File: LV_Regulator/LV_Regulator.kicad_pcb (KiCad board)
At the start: 2 copper layers, 0 parts

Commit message: Changes of PCB and Schematic files for the LV_Regulator
Removed old LDOs, added new LDOs, defined initial pcb size and I/O ports
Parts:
- added C13: ---, Capacitor_SMD:C_1206_3216Metric, F.Cu at (-29.2, 163.0)
- added C14: ---, Capacitor_SMD:C_1206_3216Metric, F.Cu at (-29.2, 166.3)
- added C15: ---, Capacitor_SMD:C_1206_3216Metric, F.Cu at (-29.2, 169.7)
- added C16: ---, Capacitor_SMD:C_1206_3216Metric, F.Cu at (-29.2, 173.0)
- added C17: 0.1uF, Capacitor_SMD:C_1206_3216Metric, F.Cu at (-29.2, 176.4)
- added C18: 100nF, Capacitor_SMD:C_1206_3216Metric, F.Cu at (-29.2, 179.7)
- added C19: 100nF, Capacitor_SMD:C_1206_3216Metric, F.Cu at (-23.5, 163.0)
- added C20: 100nF, Capacitor_SMD:C_1206_3216Metric, F.Cu at (-23.5, 166.3)
- added C21: 10uF, Capacitor_SMD:C_1206_3216Metric, F.Cu at (-23.5, 169.7)
- added C22: 100nF, Capacitor_SMD:C_1206_3216Metric, F.Cu at (-23.5, 173.0)
- added C23: 100nF, Capacitor_SMD:C_1206_3216Metric, F.Cu at (-23.5, 176.4)
- added C24: 100nF, Capacitor_SMD:C_1206_3216Metric, F.Cu at (-34.8, 126.9)
- added C25: 80uF, Capacitor_SMD:C_1206_3216Metric, F.Cu at (-34.8, 130.3)
- added C26: 40uF, Capacitor_SMD:C_1206_3216Metric, F.Cu at (-34.8, 133.6)
- added C27: 100nF, Capacitor_SMD:C_1206_3216Metric, F.Cu at (-34.8, 137.0)
- added C28: 100nF, Capacitor_SMD:C_1206_3216Metric, F.Cu at (-34.8, 140.3)
- added C29: 100nF, Capacitor_SMD:C_1206_3216Metric, F.Cu at (-34.8, 143.7)
- added C30: 40uF, Capacitor_SMD:C_1206_3216Metric, F.Cu at (-34.8, 147.0)
- added C31: 160uF, ul_UCZ1J181MNQ1MS:CAP_UCD_12P5X13P5_NCH, F.Cu at (-0.66, 151.6)
- added C32: 1uF, Capacitor_SMD:C_1206_3216Metric, F.Cu at (-34.8, 150.4)
- added C33: 1uF, Capacitor_SMD:C_1206_3216Metric, F.Cu at (-34.8, 153.7)
- added D6: LED, Diode_SMD:D_1206_3216Metric_Pad1.42x1.75mm_HandSolder, F.Cu at (-21.0, 146.8)
- added D7: LED, Diode_SMD:D_1206_3216Metric_Pad1.42x1.75mm_HandSolder, F.Cu at (-21.0, 150.2)
- added J1: 430450400, microfit-4pin:CONN_SD-43045-001_04_MOL, F.Cu at (208.3, 127.4)
- added J2: 430450800, microfit-8pin:CONN_SD-43045-001_08_MOL, F.Cu at (212.4, 63.0)
- added J3: 430450400, microfit-4pin:CONN_SD-43045-001_04_MOL, F.Cu at (188.8, 127.4)
- added J4: 430450800, microfit-8pin:CONN_SD-43045-001_08_MOL, F.Cu at (81.6, 72.0)
- added J6: 2169890001, USB_C:MOLEX_2169890001, F.Cu at (218.5, 107.5)
- added JP1: BOOT0, Jumper:SolderJumper-3_P1.3mm_Open_Pad1.0x1.5mm, F.Cu at (-34.8, 163.1)
- added JP10: SolderJumper_3_Open, Jumper:SolderJumper-3_P1.3mm_Open_Pad1.0x1.5mm, F.Cu at (10.5, 145.7)
- added JP11: SolderJumper_3_Open, Jumper:SolderJumper-3_P1.3mm_Open_Pad1.0x1.5mm, F.Cu at (10.5, 149.6)
- added JP12: SolderJumper_3_Open, Jumper:SolderJumper-3_P1.3mm_Open_Pad1.0x1.5mm, F.Cu at (10.5, 153.4)
- added JP13: SolderJumper_3_Open, Jumper:SolderJumper-3_P1.3mm_Open_Pad1.0x1.5mm, F.Cu at (10.5, 157.2)
- added JP2: ADR3, Jumper:SolderJumper-3_P1.3mm_Open_Pad1.0x1.5mm, F.Cu at (-34.8, 166.9)
- added JP3: BOOT1, Jumper:SolderJumper-3_P1.3mm_Open_Pad1.0x1.5mm, F.Cu at (-34.8, 170.8)
- added JP4: ADR2, Jumper:SolderJumper-3_P1.3mm_Open_Pad1.0x1.5mm, F.Cu at (-34.8, 174.6)
- added JP5: RESET, Jumper:SolderJumper-2_P1.3mm_Open_Pad1.0x1.5mm, F.Cu at (-29.8, 189.8)
- added JP6: ADR1, Jumper:SolderJumper-3_P1.3mm_Open_Pad1.0x1.5mm, F.Cu at (-34.8, 178.4)
- added JP7: ADR3, Jumper:SolderJumper-3_P1.3mm_Open_Pad1.0x1.5mm, F.Cu at (-34.8, 182.3)
- added JP8: ADR3, Jumper:SolderJumper-3_P1.3mm_Open_Pad1.0x1.5mm, F.Cu at (-34.8, 186.1)
- added L1: 10uH, Inductor_SMD:L_APV_APH1770, F.Cu at (0.30, 134.6)
- added Q1: BC807, Package_TO_SOT_SMD:SOT-23W_Handsoldering, F.Cu at (37.9, 122.0)
- added R10: 1M, Resistor_SMD:R_1206_3216Metric, F.Cu at (-29.2, 126.9)
- added R11: 10, Resistor_SMD:R_1206_3216Metric, F.Cu at (-29.2, 130.2)
- added R118: 27R, Resistor_SMD:R_1206_3216Metric_Pad1.30x1.75mm_HandSolder, F.Cu at (-17.7, 163.0)
- added R119: 27R, Resistor_SMD:R_1206_3216Metric_Pad1.30x1.75mm_HandSolder, F.Cu at (-17.7, 166.3)
- added R12: 5m, Resistor_SMD:R_1206_3216Metric, F.Cu at (-29.2, 133.5)
- added R120: 1K5, Resistor_SMD:R_1206_3216Metric_Pad1.30x1.75mm_HandSolder, F.Cu at (-17.7, 169.6)
- added R121: 5K1, Resistor_SMD:R_1206_3216Metric_Pad1.30x1.75mm_HandSolder, F.Cu at (-17.7, 172.9)
- added R122: 5K1, Resistor_SMD:R_1206_3216Metric_Pad1.30x1.75mm_HandSolder, F.Cu at (-17.7, 176.2)
- added R13: 10, Resistor_SMD:R_1206_3216Metric, F.Cu at (-29.2, 136.8)
- added R14: 1M, Resistor_SMD:R_1206_3216Metric, F.Cu at (-29.2, 140.2)
- added R15: 311k, Resistor_SMD:R_1206_3216Metric, F.Cu at (-29.2, 143.5)
- added R16: 22k, Resistor_SMD:R_1206_3216Metric, F.Cu at (-23.6, 126.9)
- added R31: 67k, Resistor_SMD:R_1206_3216Metric, F.Cu at (-23.6, 130.2)
- added R32: 57k, Resistor_SMD:R_1206_3216Metric, F.Cu at (-23.6, 133.5)
- added R33: 50k, Resistor_SMD:R_1206_3216Metric, F.Cu at (-23.6, 136.8)
- added R34: 100k, Resistor_SMD:R_1206_3216Metric, F.Cu at (-23.6, 140.2)
- added R35: 80k, Resistor_SMD:R_1206_3216Metric, F.Cu at (-23.6, 143.5)
- added R36: 132k, Resistor_SMD:R_1206_3216Metric, F.Cu at (-18.0, 126.9)
- added R37: 115k, Resistor_SMD:R_1206_3216Metric, F.Cu at (-18.0, 130.2)
- added R38: 1k, Resistor_SMD:R_1206_3216Metric, F.Cu at (-18.0, 133.5)
- added R39: 22k, Resistor_SMD:R_1206_3216Metric, F.Cu at (-18.0, 136.8)
- added R40: 1k, Resistor_SMD:R_1206_3216Metric, F.Cu at (-18.0, 140.2)
- added R41: 10k, Resistor_SMD:R_1206_3216Metric, F.Cu at (-18.0, 143.5)
- added R42: 10k, Resistor_SMD:R_1206_3216Metric, F.Cu at (-12.4, 126.9)
- added R43: ---, Resistor_SMD:R_1206_3216Metric, F.Cu at (-12.4, 130.2)
- added R44: ---, Resistor_SMD:R_1206_3216Metric, F.Cu at (-12.4, 133.5)
- added R45: ---, Resistor_SMD:R_1206_3216Metric, F.Cu at (-12.4, 136.8)
- added R46: ---, Resistor_SMD:R_1206_3216Metric, F.Cu at (-12.4, 140.2)
- added R47: 2.2k, Resistor_SMD:R_1206_3216Metric, F.Cu at (-12.4, 143.5)
- added U1: ADM2483xRW, Package_SO:SOIC-16W_7.5x10.3mm_P1.27mm, F.Cu at (178.5, 111.0)
- added U10: 25CSM04xxSN, Package_SO:SOIC-8_3.9x4.9mm_P1.27mm, F.Cu at (174.5, 94.5)
- added U2: MCP1826T-ADJE_DC, MCP1826T-ADJE_DC:SOT230P700X180-6N, F.Cu at (3.10, 165.2)
- added U3: MCP1826T-ADJE_DC, MCP1826T-ADJE_DC:SOT230P700X180-6N, F.Cu at (3.10, 173.1)
- added U4: STM32F103C8Tx, Package_QFP:LQFP-48_7x7mm_P0.5mm, F.Cu at (195.0, 92.5)
- added U5: BQ25858QWRRVRQ1, ul_BQ25858QWRRVRQ1:RRV0036B-IPC_A, F.Cu at (45.5, 167.0)
- added U6: CSD19506KTT, CSD19506KTT:DDPAK&slash_TO-263_KTT_TEX, F.Cu at (-31.7, 114.6)
- added U7: CSD19506KTT, CSD19506KTT:DDPAK&slash_TO-263_KTT_TEX, F.Cu at (-19.8, 114.6)
- added U8: CSD19506KTT, CSD19506KTT:DDPAK&slash_TO-263_KTT_TEX, F.Cu at (-7.86, 114.6)
- added U9: CSD19506KTT, CSD19506KTT:DDPAK&slash_TO-263_KTT_TEX, F.Cu at (4.06, 114.6)
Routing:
- added copper zone on B.Cu, net (none)
- added copper zone on F.Cu, net (none)
- added copper zone on In1.Cu, net (none)
- added copper zone on In2.Cu, net (none)
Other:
- board outline added: 150 x 100 mm
- copper layers 2 -> 4

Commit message: PCB Layout definitions part 2
Added isolation keepouts
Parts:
- removed C13, C14, C15, C16: ---, Capacitor_SMD:C_1206_3216Metric
- removed C17: 0.1uF, Capacitor_SMD:C_1206_3216Metric
- removed C18, C19, C20, C22, C23, C24, C27, C28, C29: 100nF, Capacitor_SMD:C_1206_3216Metric
- removed C21: 10uF, Capacitor_SMD:C_1206_3216Metric
- removed C25: 80uF, Capacitor_SMD:C_1206_3216Metric
- removed C26, C30: 40uF, Capacitor_SMD:C_1206_3216Metric
- removed C31: 160uF, ul_UCZ1J181MNQ1MS:CAP_UCD_12P5X13P5_NCH
- removed C32, C33: 1uF, Capacitor_SMD:C_1206_3216Metric
- removed D6, D7: LED, Diode_SMD:D_1206_3216Metric_Pad1.42x1.75mm_HandSolder
- removed J1, J3: 430450400, microfit-4pin:CONN_SD-43045-001_04_MOL
- removed J2, J4: 430450800, microfit-8pin:CONN_SD-43045-001_08_MOL
- removed J6: 2169890001, USB_C:MOLEX_2169890001
- removed JP1: BOOT0, Jumper:SolderJumper-3_P1.3mm_Open_Pad1.0x1.5mm
- removed JP10, JP11, JP12, JP13: SolderJumper_3_Open, Jumper:SolderJumper-3_P1.3mm_Open_Pad1.0x1.5mm
- removed JP2, JP7, JP8: ADR3, Jumper:SolderJumper-3_P1.3mm_Open_Pad1.0x1.5mm
- removed JP3: BOOT1, Jumper:SolderJumper-3_P1.3mm_Open_Pad1.0x1.5mm
- removed JP4: ADR2, Jumper:SolderJumper-3_P1.3mm_Open_Pad1.0x1.5mm
- removed JP5: RESET, Jumper:SolderJumper-2_P1.3mm_Open_Pad1.0x1.5mm
- removed JP6: ADR1, Jumper:SolderJumper-3_P1.3mm_Open_Pad1.0x1.5mm
- removed L1: 10uH, Inductor_SMD:L_APV_APH1770
- removed Q1: BC807, Package_TO_SOT_SMD:SOT-23W_Handsoldering
- removed R10, R14: 1M, Resistor_SMD:R_1206_3216Metric
- removed R11, R13: 10, Resistor_SMD:R_1206_3216Metric
- removed R118, R119: 27R, Resistor_SMD:R_1206_3216Metric_Pad1.30x1.75mm_HandSolder
- removed R12: 5m, Resistor_SMD:R_1206_3216Metric
- removed R120: 1K5, Resistor_SMD:R_1206_3216Metric_Pad1.30x1.75mm_HandSolder
- removed R121, R122: 5K1, Resistor_SMD:R_1206_3216Metric_Pad1.30x1.75mm_HandSolder
- removed R15: 311k, Resistor_SMD:R_1206_3216Metric
- removed R16, R39: 22k, Resistor_SMD:R_1206_3216Metric
- removed R31: 67k, Resistor_SMD:R_1206_3216Metric
- removed R32: 57k, Resistor_SMD:R_1206_3216Metric
- removed R33: 50k, Resistor_SMD:R_1206_3216Metric
- removed R34: 100k, Resistor_SMD:R_1206_3216Metric
- removed R35: 80k, Resistor_SMD:R_1206_3216Metric
- removed R36: 132k, Resistor_SMD:R_1206_3216Metric
- removed R37: 115k, Resistor_SMD:R_1206_3216Metric
- removed R38, R40: 1k, Resistor_SMD:R_1206_3216Metric
- removed R41, R42: 10k, Resistor_SMD:R_1206_3216Metric
- removed R43, R44, R45, R46: ---, Resistor_SMD:R_1206_3216Metric
- removed R47: 2.2k, Resistor_SMD:R_1206_3216Metric
- removed U1: ADM2483xRW, Package_SO:SOIC-16W_7.5x10.3mm_P1.27mm
- removed U10: 25CSM04xxSN, Package_SO:SOIC-8_3.9x4.9mm_P1.27mm
- removed U2, U3: MCP1826T-ADJE_DC, MCP1826T-ADJE_DC:SOT230P700X180-6N
- removed U4: STM32F103C8Tx, Package_QFP:LQFP-48_7x7mm_P0.5mm
- removed U5: BQ25858QWRRVRQ1, ul_BQ25858QWRRVRQ1:RRV0036B-IPC_A
- removed U6, U7, U8, U9: CSD19506KTT, CSD19506KTT:DDPAK&slash_TO-263_KTT_TEX
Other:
- board text added: "BACK"
- board text added: "FRONT"
- board text added: "L"
- board text added: "R"
- board text added: "UP"

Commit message: Halfway Push of adding 3D models to PCB layout components
Pushing with components left to add to finish on main PC
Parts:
- added C1: 100nF, Capacitor_SMD:C_1206_3216Metric_Pad1.33x1.80mm_HandSolder, F.Cu at (63.9, 150.5)
- added C10: 10uF, Capacitor_SMD:C_1206_3216Metric_Pad1.33x1.80mm_HandSolder, F.Cu at (-9.40, 211.9)
- added C11: 47uF, Capacitor_SMD:C_1206_3216Metric_Pad1.33x1.80mm_HandSolder, F.Cu at (-9.40, 215.2)
- added C12: 22uF, Capacitor_SMD:C_1206_3216Metric_Pad1.33x1.80mm_HandSolder, F.Cu at (-9.40, 218.6)
- added C13: 100nF, Capacitor_SMD:C_1206_3216Metric_Pad1.33x1.80mm_HandSolder, F.Cu at (68.3, 172.6)
- added C14: 100nF, Capacitor_SMD:C_1206_3216Metric_Pad1.33x1.80mm_HandSolder, F.Cu at (68.3, 176.0)
- added C15: 8pF, Capacitor_SMD:C_1206_3216Metric_Pad1.33x1.80mm_HandSolder, F.Cu at (68.3, 179.3)
- added C16: 12pF, Capacitor_SMD:C_1206_3216Metric_Pad1.33x1.80mm_HandSolder, F.Cu at (68.3, 182.7)
- added C17: 100nF, Capacitor_SMD:C_1206_3216Metric_Pad1.33x1.80mm_HandSolder, F.Cu at (68.3, 186.0)
- added C18: 100nF, Capacitor_SMD:C_1206_3216Metric_Pad1.33x1.80mm_HandSolder, F.Cu at (74.3, 172.6)
- added C19: 0.1uF, Capacitor_SMD:C_1206_3216Metric_Pad1.33x1.80mm_HandSolder, F.Cu at (74.3, 176.0)
- added C2: 100nF, Capacitor_SMD:C_1206_3216Metric_Pad1.33x1.80mm_HandSolder, F.Cu at (63.9, 153.9)
- added C20: 8pF, Capacitor_SMD:C_1206_3216Metric_Pad1.33x1.80mm_HandSolder, F.Cu at (74.3, 179.3)
- added C21: 12pF, Capacitor_SMD:C_1206_3216Metric_Pad1.33x1.80mm_HandSolder, F.Cu at (74.3, 182.7)
- added C22: 100nF, Capacitor_SMD:C_1206_3216Metric_Pad1.33x1.80mm_HandSolder, F.Cu at (74.3, 186.0)
- added C23: 10uF, Capacitor_SMD:C_1206_3216Metric_Pad1.33x1.80mm_HandSolder, F.Cu at (80.3, 172.6)
- added C24: 100nF, Capacitor_SMD:C_1206_3216Metric_Pad1.33x1.80mm_HandSolder, F.Cu at (80.3, 176.0)
- added C25: 100nF, Capacitor_SMD:C_1206_3216Metric_Pad1.33x1.80mm_HandSolder, F.Cu at (80.3, 179.3)
- added C26: 100nF, Capacitor_SMD:C_1206_3216Metric, F.Cu at (-15.5, 138.2)
- added C27: 100nF, Capacitor_SMD:C_1206_3216Metric, F.Cu at (-15.5, 141.6)
- added C28: 4.7uF, Capacitor_SMD:C_1206_3216Metric, F.Cu at (-15.5, 144.9)
- added C29: 1uF, Capacitor_SMD:C_1206_3216Metric, F.Cu at (-15.5, 148.3)
- added C3: 0.1uF, Capacitor_SMD:C_1206_3216Metric_Pad1.33x1.80mm_HandSolder, F.Cu at (63.9, 157.2)
- added C30: 1uF, Capacitor_SMD:C_1206_3216Metric, F.Cu at (-15.5, 151.6)
- added C31: 56uF, Capacitor_SMD:CP_Elec_10x12.5, F.Cu at (32.6, 142.6)
- added C32: 47uF, Capacitor_SMD:CP_Elec_10x10, F.Cu at (18.4, 142.5)
- added C33: 47uF, Capacitor_SMD:CP_Elec_10x10, F.Cu at (18.4, 154.3)
- added C34: 180uF, ul_UCZ1J181MNQ1MS:CAP_UCD_12P5X13P5_NCH, F.Cu at (20.0, 167.9)
- added C35: 100nF, Capacitor_SMD:C_1206_3216Metric, F.Cu at (-15.5, 155.0)
- added C36: 100nF, Capacitor_SMD:C_1206_3216Metric, F.Cu at (-15.5, 158.3)
- added C37: 4.7uF, Capacitor_SMD:C_1206_3216Metric, F.Cu at (-15.5, 161.7)
- added C4: 10uF, Capacitor_SMD:C_1206_3216Metric_Pad1.33x1.80mm_HandSolder, F.Cu at (63.9, 160.6)
- added C5: 0.1uF, Capacitor_SMD:C_1206_3216Metric_Pad1.33x1.80mm_HandSolder, F.Cu at (63.9, 163.9)
- added C6: 10uF, Capacitor_SMD:C_1206_3216Metric_Pad1.33x1.80mm_HandSolder, F.Cu at (63.9, 167.3)
- added C7: 10uF, Capacitor_SMD:C_1206_3216Metric_Pad1.33x1.80mm_HandSolder, F.Cu at (-9.40, 201.8)
- added C8: 47uF, Capacitor_SMD:C_1206_3216Metric_Pad1.33x1.80mm_HandSolder, F.Cu at (-9.40, 205.2)
- added C9: 22uF, Capacitor_SMD:C_1206_3216Metric_Pad1.33x1.80mm_HandSolder, F.Cu at (-9.40, 208.5)
- added D1: 1N4148, Diode_SMD:D_1206_3216Metric_Pad1.42x1.75mm_HandSolder, F.Cu at (82.8, 162.6)
- added D2: SS14, SS14:CR_SMA_403AE_OSI, F.Cu at (-1.71, 202.5)
- added D3: SS14, SS14:CR_SMA_403AE_OSI, F.Cu at (-1.71, 207.1)
- added D4: SS14, SS14:CR_SMA_403AE_OSI, F.Cu at (-1.71, 211.7)
- added D5: SS14, SS14:CR_SMA_403AE_OSI, F.Cu at (-1.71, 216.3)
- added D6: D_Schottky, V1FM10-M3/H:SODFL3718X108N, F.Cu at (36.8, 161.9)
- added D7: D_Schottky, V1FM10-M3/H:SODFL3718X108N, F.Cu at (36.8, 165.1)
- added D8: LED, Diode_SMD:D_1206_3216Metric_Pad1.42x1.75mm_HandSolder, F.Cu at (36.1, 150.3)
- added D9: LED, Diode_SMD:D_1206_3216Metric_Pad1.42x1.75mm_HandSolder, F.Cu at (36.1, 153.7)
- added F1: 8A, Fuse:Fuse_1206_3216Metric_Pad1.42x1.75mm_HandSolder, F.Cu at (69.9, 150.5)
- added F2: 10A, Fuse:Fuse_1206_3216Metric_Pad1.42x1.75mm_HandSolder, F.Cu at (69.9, 153.8)
- added F3: 1A, Fuse:Fuse_1206_3216Metric_Pad1.42x1.75mm_HandSolder, F.Cu at (-15.4, 201.8)
- added F4: 1A, Fuse:Fuse_1206_3216Metric_Pad1.42x1.75mm_HandSolder, F.Cu at (-15.4, 205.1)
- added IC1: UCC12040DVE, LIB_UCC12040DVE:SOIC127P1030X265-16N, F.Cu at (79.3, 154.9)
- added IC2: MIC29152WU, MIC29152WU:MIC29152WU, F.Cu at (-11.4, 190.1)
- added IC3: MIC29152WU, MIC29152WU:MIC29152WU, F.Cu at (2.41, 190.1)
- added J1: 430450400, microfit-4pin:CONN_SD-43045-001_04_MOL, F.Cu at (68.3, 139.1)
- added J2: 430450400, microfit-4pin:CONN_SD-43045-001_04_MOL, F.Cu at (81.4, 139.1)
- added J3: 430450800, microfit-8pin:CONN_SD-43045-001_08_MOL, F.Cu at (55.2, 139.1)
- added J4: 430450800, microfit-8pin:CONN_SD-43045-001_08_MOL, F.Cu at (55.2, 153.5)
- added J5: SWD, Connector_PinHeader_2.54mm:PinHeader_1x04_P2.54mm_Vertical, F.Cu at (61.9, 203.9)
- added J6: 2169890001, USB_C:MOLEX_2169890001, F.Cu at (68.9, 213.6)
- added JP1: WP, Jumper:SolderJumper-3_P1.3mm_Open_RoundedPad1.0x1.5mm, F.Cu at (62.4, 172.7)
- added JP10: SolderJumper_3_Open, Jumper:SolderJumper-3_P1.3mm_Open_RoundedPad1.0x1.5mm, F.Cu at (31.1, 162.0)
- added JP11: SolderJumper_3_Open, Jumper:SolderJumper-3_P1.3mm_Open_RoundedPad1.0x1.5mm, F.Cu at (31.1, 165.9)
- added JP12: SolderJumper_3_Open, Jumper:SolderJumper-3_P1.3mm_Open_Pad1.0x1.5mm, F.Cu at (31.1, 169.7)
- added JP13: SolderJumper_3_Open, Jumper:SolderJumper-3_P1.3mm_Open_RoundedPad1.0x1.5mm, F.Cu at (31.1, 173.5)
- added JP2: RESET, Jumper:SolderJumper-2_P1.3mm_Open_RoundedPad1.0x1.5mm, F.Cu at (54.2, 210.8)
- added JP3: BOOT0, Jumper:SolderJumper-3_P1.3mm_Open_RoundedPad1.0x1.5mm, F.Cu at (62.4, 176.6)
- added JP4: BOOT1, Jumper:SolderJumper-3_P1.3mm_Open_RoundedPad1.0x1.5mm, F.Cu at (62.4, 180.4)
- added JP5: ADR3, Jumper:SolderJumper-3_P1.3mm_Open_RoundedPad1.0x1.5mm, F.Cu at (62.4, 184.2)
- added JP6: ADR3, Jumper:SolderJumper-3_P1.3mm_Open_RoundedPad1.0x1.5mm, F.Cu at (62.4, 188.1)
- added JP7: ADR3, Jumper:SolderJumper-3_P1.3mm_Open_RoundedPad1.0x1.5mm, F.Cu at (62.4, 191.9)
- added JP8: ADR2, Jumper:SolderJumper-3_P1.3mm_Open_RoundedPad1.0x1.5mm, F.Cu at (62.4, 195.8)
- added JP9: ADR1, Jumper:SolderJumper-3_P1.3mm_Open_RoundedPad1.0x1.5mm, F.Cu at (62.4, 199.6)
- added K1: 41.52.9.005.0010, LIB_41.52.9.005.0010:415290050010, F.Cu at (45.8, 130.5)
- added L1: 10uH, Inductor_SMD:L_APV_APH1770, F.Cu at (-2.83, 169.1)
- added LED1: 5V_INT, LED_SMD:LED_1206_3216Metric_Pad1.42x1.75mm_HandSolder, F.Cu at (68.3, 189.4)
- added LED10: RX, LED_SMD:LED_1206_3216Metric_Pad1.42x1.75mm_HandSolder, F.Cu at (80.3, 192.8)
- added LED11: TX, LED_SMD:LED_1206_3216Metric_Pad1.42x1.75mm_HandSolder, F.Cu at (80.3, 196.2)
- added LED12: RUN, LED_SMD:LED_1206_3216Metric_Pad1.42x1.75mm_HandSolder, F.Cu at (80.3, 199.6)
- added LED2: 3V3_INT, LED_SMD:LED_1206_3216Metric_Pad1.42x1.75mm_HandSolder, F.Cu at (68.3, 192.8)
- added LED3: 5V_EXT, LED_SMD:LED_1206_3216Metric_Pad1.42x1.75mm_HandSolder, F.Cu at (68.3, 196.2)
- added LED4: 3V3_EXT, LED_SMD:LED_1206_3216Metric_Pad1.42x1.75mm_HandSolder, F.Cu at (68.3, 199.6)
- added LED5: REL, LED_SMD:LED_1206_3216Metric_Pad1.42x1.75mm_HandSolder, F.Cu at (74.3, 189.4)
- added LED6: 5V, LED_SMD:LED_1206_3216Metric_Pad1.42x1.75mm_HandSolder, F.Cu at (74.3, 192.8)
- added LED7: 3V3, LED_SMD:LED_1206_3216Metric_Pad1.42x1.75mm_HandSolder, F.Cu at (74.3, 196.2)
- added LED8: OK, LED_SMD:LED_1206_3216Metric_Pad1.42x1.75mm_HandSolder, F.Cu at (74.3, 199.6)
- added LED9: ERR, LED_SMD:LED_1206_3216Metric_Pad1.42x1.75mm_HandSolder, F.Cu at (80.3, 189.4)
- added Q1: BC807, Package_TO_SOT_SMD:SOT-23W_Handsoldering, F.Cu at (76.3, 163.4)
- added R1: ---, Resistor_SMD:R_1206_3216Metric_Pad1.30x1.75mm_HandSolder, F.Cu at (69.9, 157.1)
- added R10: 270, Resistor_SMD:R_1206_3216Metric_Pad1.30x1.75mm_HandSolder, F.Cu at (44.7, 172.6)
- added R11: 130, Resistor_SMD:R_1206_3216Metric_Pad1.30x1.75mm_HandSolder, F.Cu at (44.7, 175.9)
- added R12: 270, Resistor_SMD:R_1206_3216Metric_Pad1.30x1.75mm_HandSolder, F.Cu at (44.7, 179.2)
- added R13: 130, Resistor_SMD:R_1206_3216Metric_Pad1.30x1.75mm_HandSolder, F.Cu at (44.7, 182.6)
- added R14: 130, Resistor_SMD:R_1206_3216Metric_Pad1.30x1.75mm_HandSolder, F.Cu at (44.7, 185.9)
- added R15: 270, Resistor_SMD:R_1206_3216Metric_Pad1.30x1.75mm_HandSolder, F.Cu at (44.7, 189.2)
- added R16: 130, Resistor_SMD:R_1206_3216Metric_Pad1.30x1.75mm_HandSolder, F.Cu at (44.7, 192.5)
- added R17: 130, Resistor_SMD:R_1206_3216Metric_Pad1.30x1.75mm_HandSolder, F.Cu at (50.7, 172.6)
- added R18: 130, Resistor_SMD:R_1206_3216Metric_Pad1.30x1.75mm_HandSolder, F.Cu at (50.7, 175.9)
- added R19: 130, Resistor_SMD:R_1206_3216Metric_Pad1.30x1.75mm_HandSolder, F.Cu at (50.7, 179.2)
- added R2: 120, Resistor_SMD:R_1206_3216Metric_Pad1.30x1.75mm_HandSolder, F.Cu at (69.9, 160.4)
- added R20: 130, Resistor_SMD:R_1206_3216Metric_Pad1.30x1.75mm_HandSolder, F.Cu at (50.7, 182.6)
- added R21: 130, Resistor_SMD:R_1206_3216Metric_Pad1.30x1.75mm_HandSolder, F.Cu at (50.7, 185.9)
- added R22: 5K1, Resistor_SMD:R_1206_3216Metric_Pad1.30x1.75mm_HandSolder, F.Cu at (50.7, 189.2)
- added R23: 5K1, Resistor_SMD:R_1206_3216Metric_Pad1.30x1.75mm_HandSolder, F.Cu at (50.7, 192.5)
- added R24: 10K, Resistor_SMD:R_1206_3216Metric_Pad1.30x1.75mm_HandSolder, F.Cu at (56.6, 172.6)
- added R25: 27R, Resistor_SMD:R_1206_3216Metric_Pad1.30x1.75mm_HandSolder, F.Cu at (56.6, 175.9)
- added R26: 27R, Resistor_SMD:R_1206_3216Metric_Pad1.30x1.75mm_HandSolder, F.Cu at (56.6, 179.2)
- added R27: 1K5, Resistor_SMD:R_1206_3216Metric_Pad1.30x1.75mm_HandSolder, F.Cu at (56.6, 182.6)
- added R28: 132k, Resistor_SMD:R_1206_3216Metric_Pad1.30x1.75mm_HandSolder, F.Cu at (-9.73, 138.2)
- added R29: 67k, Resistor_SMD:R_1206_3216Metric_Pad1.30x1.75mm_HandSolder, F.Cu at (-9.73, 141.5)
- added R3: ---, Resistor_SMD:R_1206_3216Metric_Pad1.30x1.75mm_HandSolder, F.Cu at (69.9, 163.8)
- added R30: 100k, Resistor_SMD:R_1206_3216Metric_Pad1.30x1.75mm_HandSolder, F.Cu at (-9.73, 144.8)
- added R31: 57k, Resistor_SMD:R_1206_3216Metric_Pad1.30x1.75mm_HandSolder, F.Cu at (-9.73, 148.2)
- added R32: 1M, Resistor_SMD:R_1206_3216Metric_Pad1.30x1.75mm_HandSolder, F.Cu at (-9.73, 151.5)
- added R33: 115k, Resistor_SMD:R_1206_3216Metric_Pad1.30x1.75mm_HandSolder, F.Cu at (-9.73, 154.8)
- added R34: 1k, Resistor_SMD:R_1206_3216Metric_Pad1.30x1.75mm_HandSolder, F.Cu at (-9.73, 158.1)
- added R35: 22k, Resistor_SMD:R_1206_3216Metric_Pad1.30x1.75mm_HandSolder, F.Cu at (-3.79, 138.2)
- added R36: 1k, Resistor_SMD:R_1206_3216Metric_Pad1.30x1.75mm_HandSolder, F.Cu at (-3.79, 141.5)
- added R37: 80k, Resistor_SMD:R_1206_3216Metric_Pad1.30x1.75mm_HandSolder, F.Cu at (-3.79, 144.8)
- added R38: 50k, Resistor_SMD:R_1206_3216Metric_Pad1.30x1.75mm_HandSolder, F.Cu at (-3.79, 148.2)
- added R39: 1M, Resistor_SMD:R_1206_3216Metric_Pad1.30x1.75mm_HandSolder, F.Cu at (-3.79, 151.5)
- added R4: 4k7, Resistor_SMD:R_1206_3216Metric_Pad1.30x1.75mm_HandSolder, F.Cu at (69.9, 167.1)
- added R40: 311k, Resistor_SMD:R_1206_3216Metric_Pad1.30x1.75mm_HandSolder, F.Cu at (-3.79, 154.8)
- added R41: 22k, Resistor_SMD:R_1206_3216Metric_Pad1.30x1.75mm_HandSolder, F.Cu at (-3.79, 158.1)
- added R42: ---, Resistor_SMD:R_1206_3216Metric_Pad1.30x1.75mm_HandSolder, F.Cu at (2.17, 138.2)
- added R43: ---, Resistor_SMD:R_1206_3216Metric_Pad1.30x1.75mm_HandSolder, F.Cu at (2.17, 141.5)
- added R44: ---, Resistor_SMD:R_1206_3216Metric_Pad1.30x1.75mm_HandSolder, F.Cu at (2.17, 144.8)
- added R45: ---, Resistor_SMD:R_1206_3216Metric_Pad1.30x1.75mm_HandSolder, F.Cu at (2.17, 148.2)
- added R46: ---, Resistor_SMD:R_1206_3216Metric_Pad1.30x1.75mm_HandSolder, F.Cu at (2.17, 151.5)
- added R47: ---, Resistor_SMD:R_1206_3216Metric_Pad1.30x1.75mm_HandSolder, F.Cu at (2.17, 154.8)
- added R48: ---, Resistor_SMD:R_1206_3216Metric_Pad1.30x1.75mm_HandSolder, F.Cu at (2.17, 158.1)
- added R49: 2.2k, Resistor_SMD:R_1206_3216Metric_Pad1.30x1.75mm_HandSolder, F.Cu at (8.12, 138.2)
- added R5: 33k, Resistor_SMD:R_1206_3216Metric_Pad1.30x1.75mm_HandSolder, F.Cu at (-15.4, 208.4)
- added R50: 5m, FCSL110R005FER:RESC50110X70N, F.Cu at (33.1, 125.3)
- added R51: 10, Resistor_SMD:R_1206_3216Metric_Pad1.30x1.75mm_HandSolder, F.Cu at (8.12, 141.5)
- added R52: 10, Resistor_SMD:R_1206_3216Metric_Pad1.30x1.75mm_HandSolder, F.Cu at (8.12, 144.8)
- added R53: 10k, Resistor_SMD:R_1206_3216Metric_Pad1.30x1.75mm_HandSolder, F.Cu at (8.12, 148.2)
- added R54: 10k, Resistor_SMD:R_1206_3216Metric_Pad1.30x1.75mm_HandSolder, F.Cu at (8.12, 151.5)
- added R6: 10k, Resistor_SMD:R_1206_3216Metric_Pad1.30x1.75mm_HandSolder, F.Cu at (-15.4, 211.8)
- added R7: 34k, Resistor_SMD:R_1206_3216Metric_Pad1.30x1.75mm_HandSolder, F.Cu at (-15.4, 215.1)
- added R8: 10K, Resistor_SMD:R_1206_3216Metric_Pad1.30x1.75mm_HandSolder, F.Cu at (-15.4, 218.4)
- added R9: 10K, Resistor_SMD:R_1206_3216Metric_Pad1.30x1.75mm_HandSolder, F.Cu at (-15.4, 221.7)
- added TP1: TestPoint, TestPoint:TestPoint_Pad_1.0x1.0mm, F.Cu at (12.8, 182.0)
- added TP10: TestPoint, TestPoint:TestPoint_Pad_1.0x1.0mm, F.Cu at (15.9, 185.0)
- added TP11: TestPoint, TestPoint:TestPoint_Pad_1.0x1.0mm, F.Cu at (15.9, 188.1)
- added TP12: TestPoint, TestPoint:TestPoint_Pad_1.0x1.0mm, F.Cu at (15.9, 191.1)
- added TP13: TestPoint, TestPoint:TestPoint_Pad_1.0x1.0mm, F.Cu at (15.9, 194.2)
- added TP14: TestPoint, TestPoint:TestPoint_Pad_1.0x1.0mm, F.Cu at (15.9, 197.2)
- added TP15: TestPoint, TestPoint:TestPoint_Pad_1.0x1.0mm, F.Cu at (15.9, 200.3)
- added TP16: TestPoint, TestPoint:TestPoint_Pad_1.0x1.0mm, F.Cu at (15.9, 203.3)
- added TP17: TestPoint, TestPoint:TestPoint_Pad_1.0x1.0mm, F.Cu at (18.9, 182.0)
- added TP18: TestPoint, TestPoint:TestPoint_Pad_1.0x1.0mm, F.Cu at (18.9, 185.0)
- added TP19: TestPoint, TestPoint:TestPoint_Pad_1.0x1.0mm, F.Cu at (18.9, 188.1)
- added TP2: TestPoint, TestPoint:TestPoint_Pad_1.0x1.0mm, F.Cu at (12.8, 185.0)
- added TP20: TestPoint, TestPoint:TestPoint_Pad_1.0x1.0mm, F.Cu at (18.9, 191.1)
- added TP21: TestPoint, TestPoint:TestPoint_Pad_1.0x1.0mm, F.Cu at (18.9, 194.2)
- added TP22: TestPoint, TestPoint:TestPoint_Pad_1.0x1.0mm, F.Cu at (18.9, 197.2)
- added TP23: TestPoint, TestPoint:TestPoint_Pad_1.0x1.0mm, F.Cu at (18.9, 200.3)
- added TP24: TestPoint, TestPoint:TestPoint_Pad_1.0x1.0mm, F.Cu at (18.9, 203.3)
- added TP25: TestPoint, TestPoint:TestPoint_Pad_1.0x1.0mm, F.Cu at (22.0, 182.0)
- added TP26: TestPoint, TestPoint:TestPoint_Pad_1.0x1.0mm, F.Cu at (22.0, 185.0)
- added TP27: TestPoint, TestPoint:TestPoint_Pad_1.0x1.0mm, F.Cu at (22.0, 188.1)
- added TP28: TestPoint, TestPoint:TestPoint_Pad_1.0x1.0mm, F.Cu at (22.0, 191.1)
- added TP29: TestPoint, TestPoint:TestPoint_Pad_1.0x1.0mm, F.Cu at (22.0, 194.2)
- added TP3: TestPoint, TestPoint:TestPoint_Pad_1.0x1.0mm, F.Cu at (12.8, 188.1)
- added TP30: TestPoint, TestPoint:TestPoint_Pad_1.0x1.0mm, F.Cu at (22.0, 197.2)
- added TP31: TestPoint, TestPoint:TestPoint_Pad_1.0x1.0mm, F.Cu at (22.0, 200.3)
- added TP32: TestPoint, TestPoint:TestPoint_Pad_1.0x1.0mm, F.Cu at (22.0, 203.3)
- added TP33: TestPoint, TestPoint:TestPoint_Pad_1.0x1.0mm, F.Cu at (25.0, 182.0)
- added TP34: TestPoint, TestPoint:TestPoint_Pad_1.0x1.0mm, F.Cu at (25.0, 185.0)
- added TP35: TestPoint, TestPoint:TestPoint_Pad_1.0x1.0mm, F.Cu at (25.0, 188.1)
- added TP36: TestPoint, TestPoint:TestPoint_Pad_1.0x1.0mm, F.Cu at (25.0, 191.1)
- added TP37: TestPoint, TestPoint:TestPoint_Pad_1.0x1.0mm, F.Cu at (25.0, 194.2)
- added TP38: TestPoint, TestPoint:TestPoint_Pad_1.0x1.0mm, F.Cu at (25.0, 197.2)
- added TP39: TestPoint, TestPoint:TestPoint_Pad_1.0x1.0mm, F.Cu at (25.0, 200.3)
- added TP4: TestPoint, TestPoint:TestPoint_Pad_1.0x1.0mm, F.Cu at (12.8, 191.1)
- added TP40: TestPoint, TestPoint:TestPoint_Pad_1.0x1.0mm, F.Cu at (25.0, 203.3)
- added TP41: TestPoint, TestPoint:TestPoint_Pad_1.0x1.0mm, F.Cu at (28.1, 182.0)
- added TP42: TestPoint, TestPoint:TestPoint_Pad_1.0x1.0mm, F.Cu at (28.1, 185.0)
- added TP43: TestPoint, TestPoint:TestPoint_Pad_1.0x1.0mm, F.Cu at (28.1, 188.1)
- added TP44: TestPoint, TestPoint:TestPoint_Pad_1.0x1.0mm, F.Cu at (28.1, 191.1)
- added TP5: TestPoint, TestPoint:TestPoint_Pad_1.0x1.0mm, F.Cu at (12.8, 194.2)
- added TP6: TestPoint, TestPoint:TestPoint_Pad_1.0x1.0mm, F.Cu at (12.8, 197.2)
- added TP7: TestPoint, TestPoint:TestPoint_Pad_1.0x1.0mm, F.Cu at (12.8, 200.3)
- added TP8: TestPoint, TestPoint:TestPoint_Pad_1.0x1.0mm, F.Cu at (12.8, 203.3)
- added TP9: TestPoint, TestPoint:TestPoint_Pad_1.0x1.0mm, F.Cu at (15.9, 182.0)
- added U1: ADM2483xRW, Package_SO:SOIC-16W_7.5x10.3mm_P1.27mm, F.Cu at (80.3, 124.9)
- added U2: STM32F103C8Tx, Package_QFP:LQFP-48_7x7mm_P0.5mm, F.Cu at (47.4, 199.8)
- added U3: 25CSM04xxSN, Package_SO:SOIC-8_3.9x4.9mm_P1.27mm, F.Cu at (46.0, 214.1)
- added U4: BQ25858QWRRVRQ1, ul_BQ25858QWRRVRQ1:RRV0036B-IPC_A, F.Cu at (29.7, 152.6)
- added U5: CSD19506KTT, CSD19506KTT:DDPAK&slash_TO-263_KTT_TEX, F.Cu at (-12.4, 125.9)
- added U6: CSD19506KTT, CSD19506KTT:DDPAK&slash_TO-263_KTT_TEX, F.Cu at (-0.48, 125.9)
- added U7: CSD19506KTT, CSD19506KTT:DDPAK&slash_TO-263_KTT_TEX, F.Cu at (11.4, 125.9)
- added U8: CSD19506KTT, CSD19506KTT:DDPAK&slash_TO-263_KTT_TEX, F.Cu at (23.4, 125.9)
- added Y1: 32.768kHz, Crystal:Crystal_SMD_EuroQuartz_EQ161-2Pin_3.2x1.5mm_HandSoldering, F.Cu at (55.4, 207.3)
- added Y2: 8MHz, Crystal:Crystal_SMD_5032-2Pin_5.0x3.2mm_HandSoldering, F.Cu at (46.9, 208.1)
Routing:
- removed copper zone on B.Cu, net (none)
- removed copper zone on F.Cu, net (none)
- removed copper zone on In1.Cu, net (none)
- removed copper zone on In2.Cu, net (none)
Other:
- board text removed: "BACK"
- board text removed: "FRONT"
- board text removed: "L"
- board text removed: "R"
- board text removed: "UP"

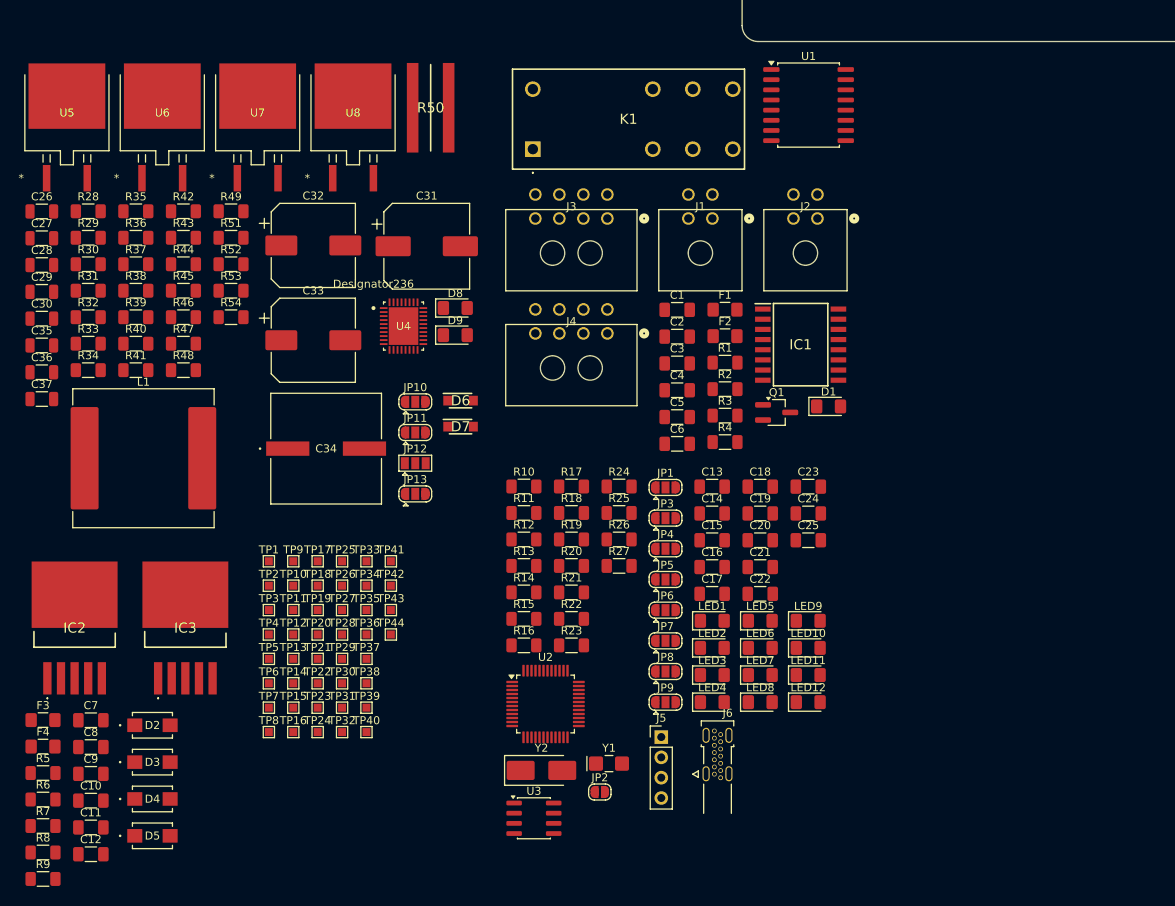
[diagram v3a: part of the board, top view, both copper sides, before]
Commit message: Added 3D models to components part 2
Modeled some Custom .step models for components whose 3D models I couldn't find, and imported the rest.
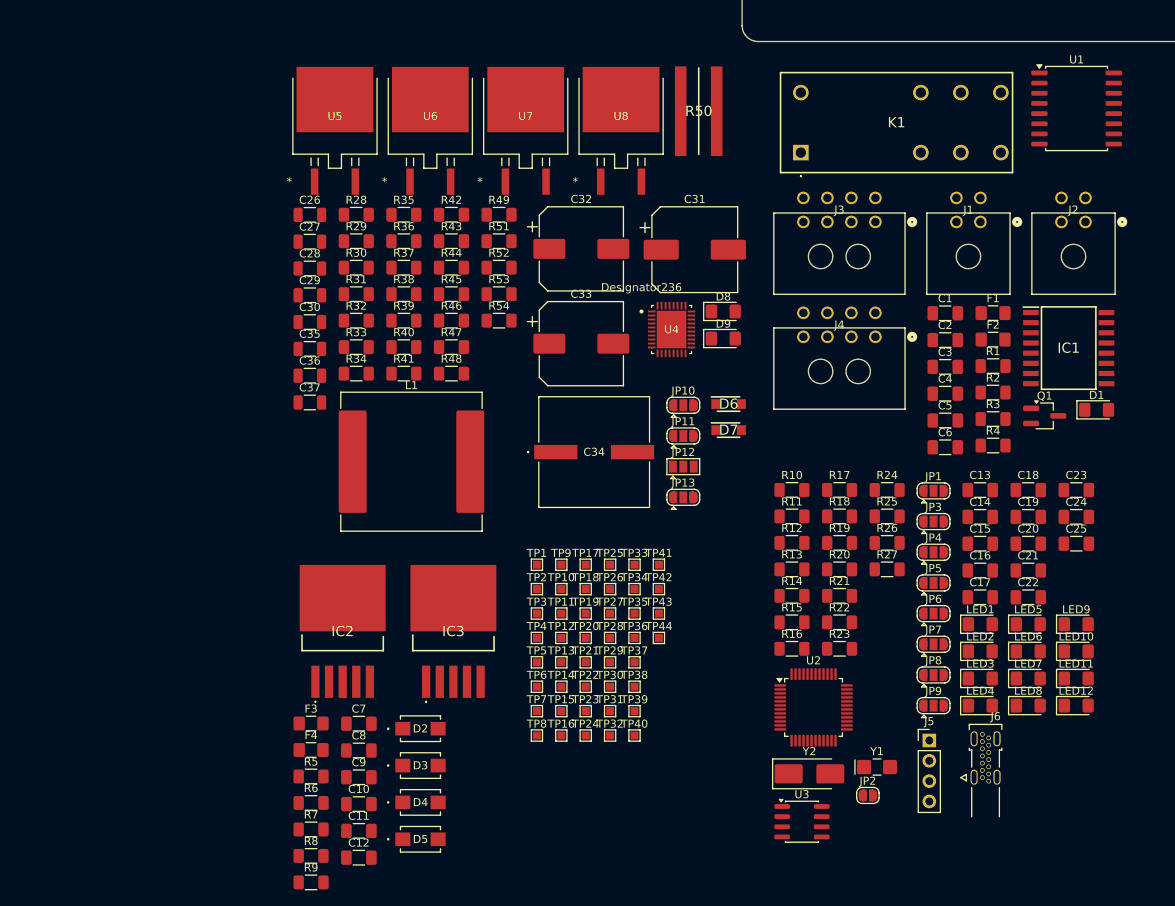
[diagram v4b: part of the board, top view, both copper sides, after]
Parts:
- moved C13 33.5 mm to (101.8, 173.1)
- moved C14 33.5 mm to (101.8, 176.4)
- moved C15 33.5 mm to (101.8, 179.8)
- moved C16 33.5 mm to (101.8, 183.1)
- moved C17 33.5 mm to (101.8, 186.5)
- moved F1 33.5 mm to (103.4, 150.9)
- moved F2 33.5 mm to (103.4, 154.3)
- moved J1 33.5 mm to (101.8, 139.6)
- moved J2 33.5 mm to (114.9, 139.6)
- moved J6 33.5 mm to (102.4, 214.1)
- moved JP1 33.5 mm to (95.9, 173.2)
- moved JP10 33.5 mm to (64.7, 162.5)
- moved JP11 33.5 mm to (64.7, 166.3)
- moved JP12 33.5 mm to (64.7, 170.1)
- moved JP13 33.5 mm to (64.7, 174.0)
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
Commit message: Initial Routing for tje LV_Regulator control portion
Changes to the schematic were made for simpler routing
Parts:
- C15, C16, C20, C21, C22, C23, C24, C25, D1, JP5, JP6, JP7, JP8, JP9, R12, R13, R17, R18, R19, R20, R21, R22, R23, R26, R27: moved to B.Cu
- C31: footprint Capacitor_SMD:CP_Elec_10x12.5 -> ul_UCZ1J181MNQ1MS:CAP_UCD_12P5X13P5_NCH
- moved D2 483.5 mm to (481.7, 25.9)
- moved D3 483.5 mm to (481.7, 30.5)
- moved D4 483.5 mm to (481.7, 35.1)
- moved D5 483.5 mm to (481.7, 39.7)
- moved F3 478.6 mm to (462.1, 23.6)
- moved F4 478.6 mm to (462.1, 26.9)
- moved R5 478.6 mm to (462.1, 30.2)
- moved R6 478.6 mm to (462.1, 33.5)
- moved R7 478.6 mm to (462.1, 36.8)
- moved R8 478.6 mm to (462.1, 40.1)
- moved R9 478.6 mm to (462.1, 43.4)
- moved C10 478.6 mm to (468.1, 33.6)
- moved C11 478.6 mm to (468.1, 37.0)
- moved C12 478.6 mm to (468.1, 40.3)
- moved C7 478.6 mm to (468.1, 23.6)
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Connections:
- net VBAT renamed +3.3V
- J1 pad 2: 3V3_EXT -> GND
- J1 pad 4: GND -> 3V3_EXT
- J2 pad 1: RS485-A -> RS485-B
- J2 pad 2: RS485-B -> RS485-A
- LED10 pad 2: DIAG_RUN -> DIAG_RX
- LED12 pad 2: DIAG_RX -> DIAG_RUN
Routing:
- net +5V_ISO: track 0.00 -> 45.6 mm
- net BAT-: track 0.00 -> 42.1 mm
- net RELEJ: track 0.00 -> 35.3 mm, vias 0 -> 2
- net SS: track 0.00 -> 30.3 mm, vias 0 -> 2
- net MISO_DOBROTO: track 0.00 -> 30.3 mm, vias 0 -> 2
- net +3.3V: track 0.00 -> 27.5 mm, vias 0 -> 9
- net RS485-RX: track 0.00 -> 24.3 mm, vias 0 -> 2
- net DIAG_RX: track 0.00 -> 24.0 mm, vias 0 -> 2
- net RS485-DIR: track 0.00 -> 23.7 mm, vias 0 -> 2
- net GND: track 0.00 -> 23.6 mm, vias 0 -> 21
- net RS485-A: track 0.00 -> 23.4 mm
- net GND_ISO: track 0.00 -> 22.8 mm, vias 0 -> 5
- net CON_DN: track 0.00 -> 21.6 mm
- net RS485-B: track 0.00 -> 21.5 mm
- net DIAG_TX: track 0.00 -> 20.9 mm, vias 0 -> 2
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- added copper zone on F.Cu, net +3.3V
- added copper zone on In2.Cu, net +5V
- added copper zone on B.Cu, net GND
- added copper zone on In1.Cu, net GND
- added copper zone on B.Cu, net GND_ISO
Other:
- board text added: "BACK"
- board text added: "FRONT"
- board text added: "L"
- board text added: "R"
- board text added: "UP"
